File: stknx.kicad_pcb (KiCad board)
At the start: 2 copper layers, 51.3 x 20.3 mm, 48 parts, among them J1 KNX, J2 PMOD, J3 VDDHV, J4 VCCCORE, J5 VDCDC, U1 STKNX

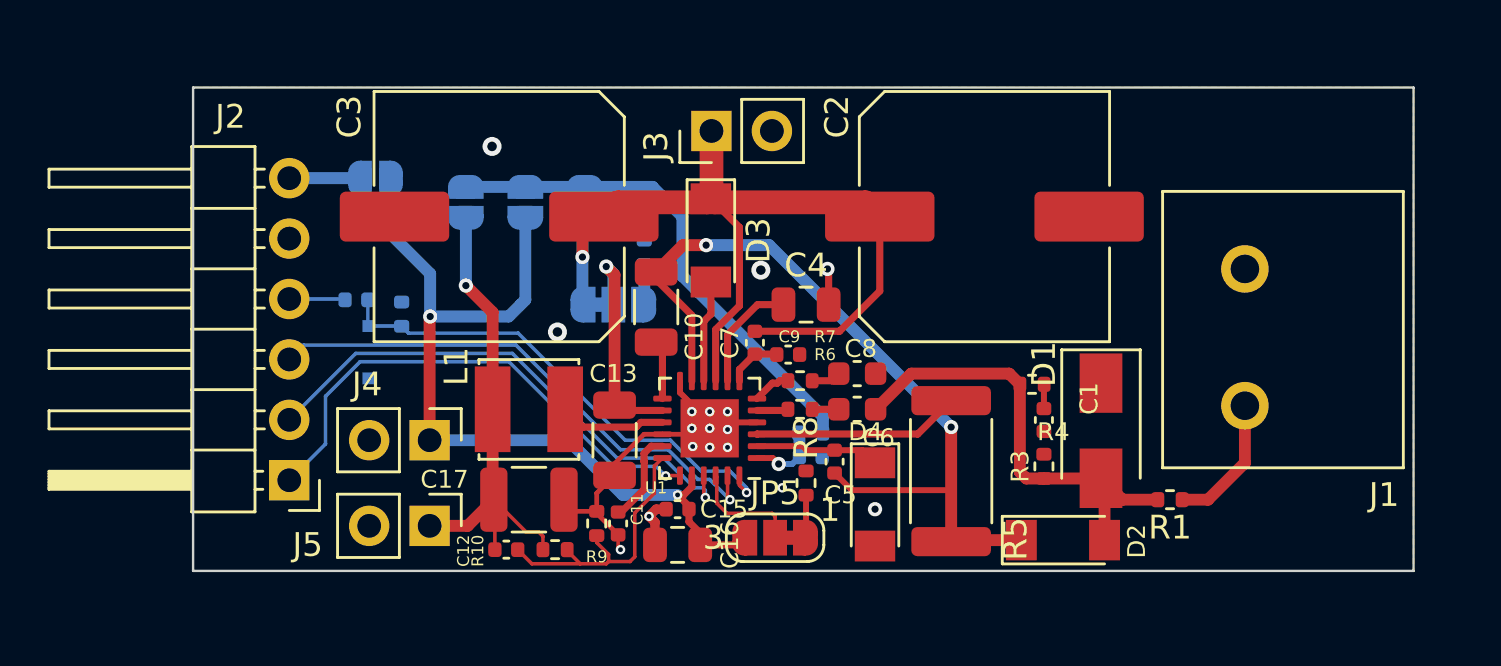
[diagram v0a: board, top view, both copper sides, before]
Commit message: reroute with jlc specs
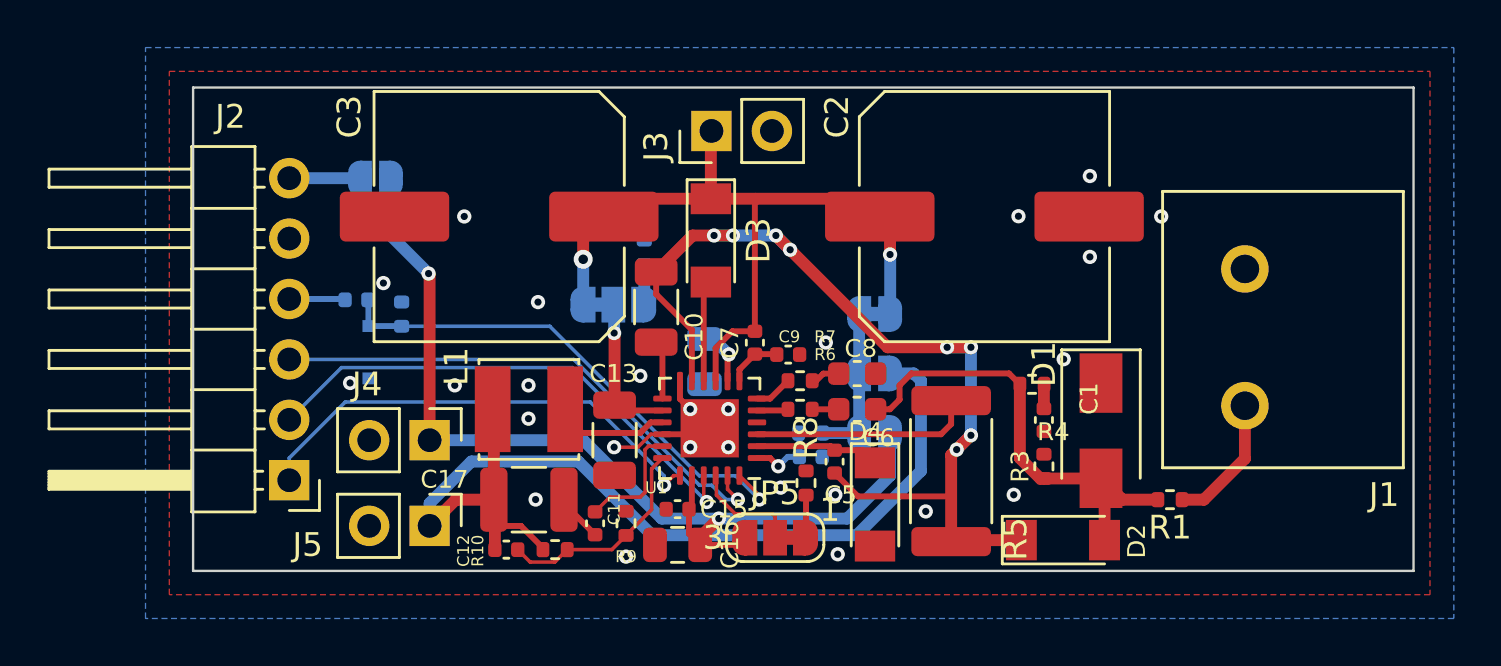
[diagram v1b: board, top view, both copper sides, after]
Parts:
- C4: moved to B.Cu
- moved JP3 18.6 mm to (183.1, 108.8), turned to 0 degrees
- moved JP4 17.6 mm to (183.1, 111.3), turned to 0 degrees
- moved JP2 13.1 mm to (183.1, 106.3), turned to 0 degrees
- moved C4 4.89 mm to (175.9, 108.3), turned to 90 degrees
- moved R9 1.23 mm to (172.6, 115.1)
- moved C11 0.97 mm to (171.3, 115.1)
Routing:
- net /VDCDC: track 20.9 -> 41.5 mm, vias 1 -> 0
- net /VDD_REGIN: track 21.2 -> 6.53 mm
- net GND: track 16.3 -> 7.72 mm, vias 17 -> 26
- net Net-(C10-Pad1): track 34.4 -> 41.3 mm, vias 2 -> 8
- net /VDDHV: track 38.5 -> 32.3 mm, vias 1 -> 2
- net /VCCCORE: track 36.3 -> 41.5 mm
- net /DCDC_IN: track 9.80 -> 6.35 mm
- net Net-(C12-Pad2): track 12.0 -> 9.12 mm
- net Net-(C4-Pad2): track 4.82 -> 2.43 mm, vias 0 -> 1
- net /KNX_VCC_OK: track 21.7 -> 20.2 mm
- net Net-(C11-Pad1): track 3.91 -> 5.03 mm
- net Net-(C18-Pad1): track 20.9 -> 21.9 mm
- net Net-(L1-Pad1): track 4.48 -> 5.23 mm
- net Net-(R5-Pad2): track 8.75 -> 9.33 mm

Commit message: via size fasching and some GND optimization
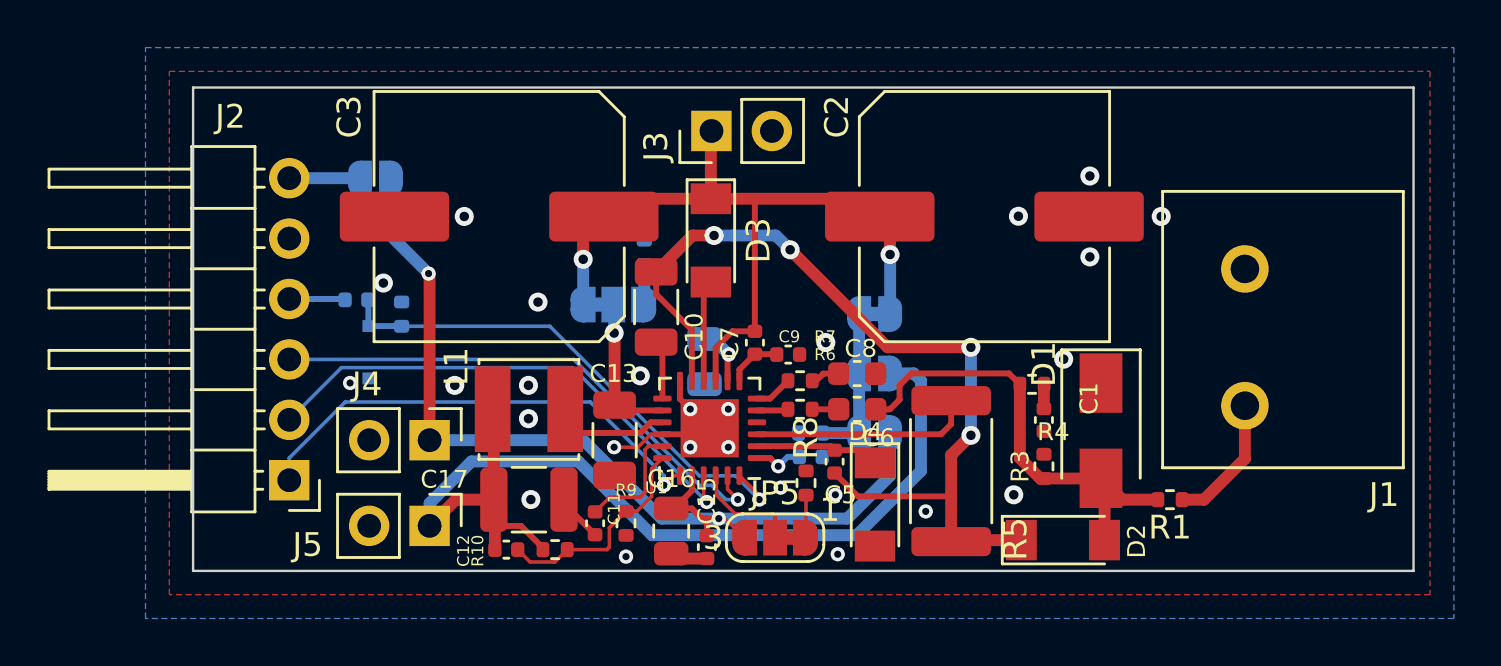
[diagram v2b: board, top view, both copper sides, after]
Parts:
- moved C15 2.01 mm to (176.0, 116.1), turned to -90 degrees
- moved C16 0.64 mm to (174.5, 115.4), turned to -90 degrees
- turned R9 to -90 degrees
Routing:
- net Net-(C10-Pad1): track 41.3 -> 37.8 mm, vias 8 -> 4
- net GND: track 7.72 -> 9.32 mm

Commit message: Silkscreen
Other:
- board text added: "3V3"
- board text added: "5V"
- board text added: "CORE"
- board text added: "DCDC"
- board text added: "DCDC Regulator Config"
- board text added: "HV"
- board text added: "Lin. Voltage"
- board text added: "Linear Regulator Input"
- board text added: "OFF"
- board text added: "Off"
- board text added: "On"
- board text added: "VCCORE Supply Enable"
- board text added: "VDCDC"
- board text added: "VDDHV"

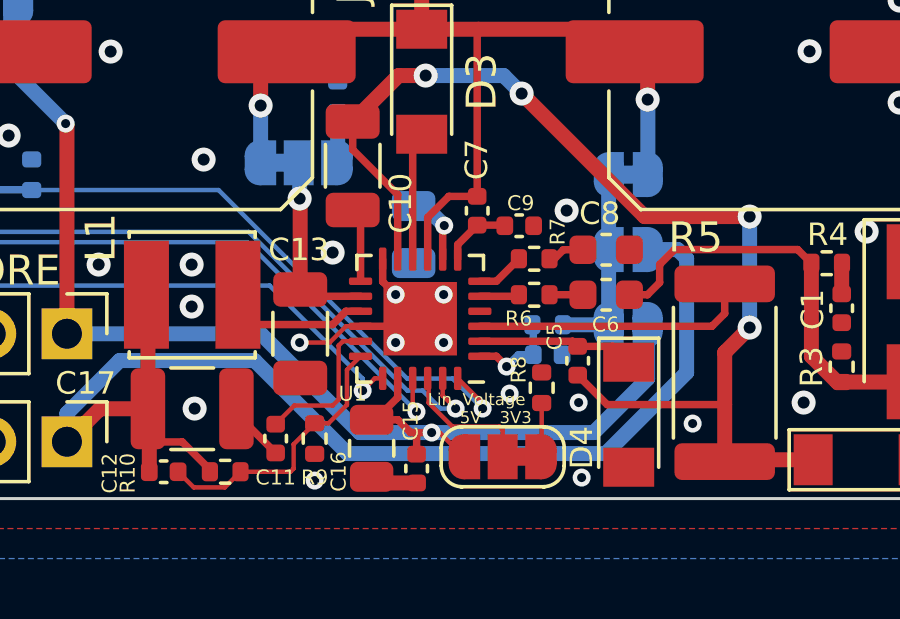
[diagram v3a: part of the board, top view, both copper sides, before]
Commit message: fix U1 pin 4 connectivity
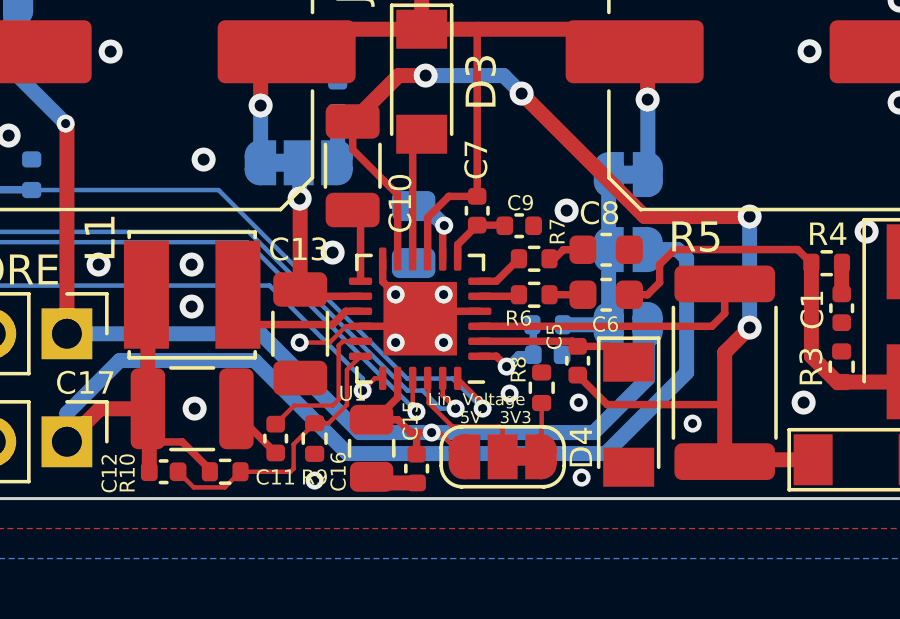
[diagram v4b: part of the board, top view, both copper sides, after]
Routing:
- net GND: track 9.32 -> 11.4 mm
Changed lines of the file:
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@@
     (effects (font (size 0.4 0.4) (thickness 0.07)))
   )
+  (segment (start 178.1375 110.85) (end 176.4 110.85) (width 0.25) (layer "F.Cu") (net 1))
   (segment (start 172.132 111.894) (end 173.132 111.894) (width 0.15) (layer "F.Cu") (net 1))
   (segment (start 174.737 116.574) (end 174.532 116.369) (width 0.5) (layer "F.Cu") (net 1))
@@
   (segment (start 171.332 115.574) (end 170.025 114.267) (width 0.25) (layer "F.Cu") (net 1))
   (segment (start 174.9 109.1125) (end 174.9 109.862) (width 0.25) (layer "F.Cu") (net 1))
+  (segment (start 176.4 110.85) (end 176.15 111.1) (width 0.25) (layer "F.Cu") (net 1))
   (segment (start 175.9 111.35) (end 176.15 111.1) (width 0.25) (layer "F.Cu") (net 1))
   (segment (start 170.025 114.267) (end 170.025 114.1) (width 0.25) (layer "F.Cu") (net 1))

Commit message: Remove default-jumpers and replace them with open jumpers to avoid the need to scratch around on that beatiful PCB
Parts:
- JP1, JP5: footprint Jumper:SolderJumper-3_P1.3mm_Bridged12_RoundedPad1.0x1.5mm_NumberLabels -> Jumper:SolderJumper-3_P1.3mm_Open_RoundedPad1.0x1.5mm_NumberLabels
- JP2: footprint Jumper:SolderJumper-2_P1.3mm_Bridged_RoundedPad1.0x1.5mm -> Jumper:SolderJumper-2_P1.3mm_Open_RoundedPad1.0x1.5mm
